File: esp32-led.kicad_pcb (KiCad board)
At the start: 2 copper layers, 28.7 x 55.6 mm, 10 parts, among them J1 LED Connector, J2 USB4125-GF-A_REVA2, J3 LED Connector, U1 SN74AHCT125D, U2 ESP32_NODEMCU

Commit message: Fixed issues, added gerber files
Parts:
- added REF**: MountingHole_4.3mm_M4_ISO14580, MountingHole:MountingHole_4.3mm_M4_ISO14580, F.Cu at (146.6, 95.2)
- added REF**: MountingHole_4.3mm_M4_ISO14580, MountingHole:MountingHole_4.3mm_M4_ISO14580, F.Cu at (146.7, 51.8)
- added REF**: MountingHole_4.3mm_M4_ISO14580, MountingHole:MountingHole_4.3mm_M4_ISO14580, F.Cu at (187.4, 95.1)
- added REF**: MountingHole_4.3mm_M4_ISO14580, MountingHole:MountingHole_4.3mm_M4_ISO14580, F.Cu at (187.4, 51.8)
- moved J1 0.32 mm to (164.6, 48.5)
- moved J3 0.20 mm to (169.7, 48.5)
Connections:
- J3 pad 1: +5V -> GND
- J3 pad 3: GND -> +5V
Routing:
- net DATA: track 28.6 -> 40.1 mm
- net +5V: track 100.5 -> 104.7 mm
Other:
- board size 28.7 x 55.6 mm -> 50.8 x 56.2 mm

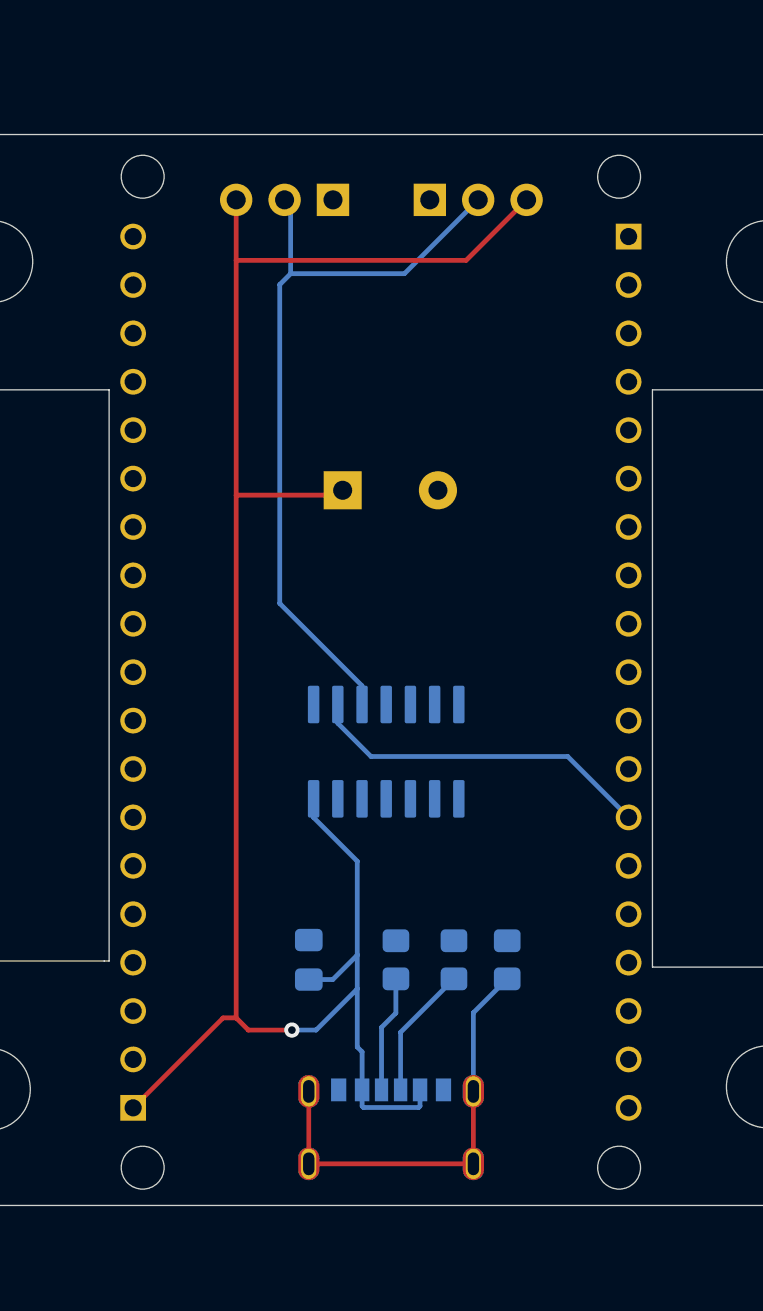
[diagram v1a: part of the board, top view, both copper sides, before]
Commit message: Chamged wrong esp32 footprint
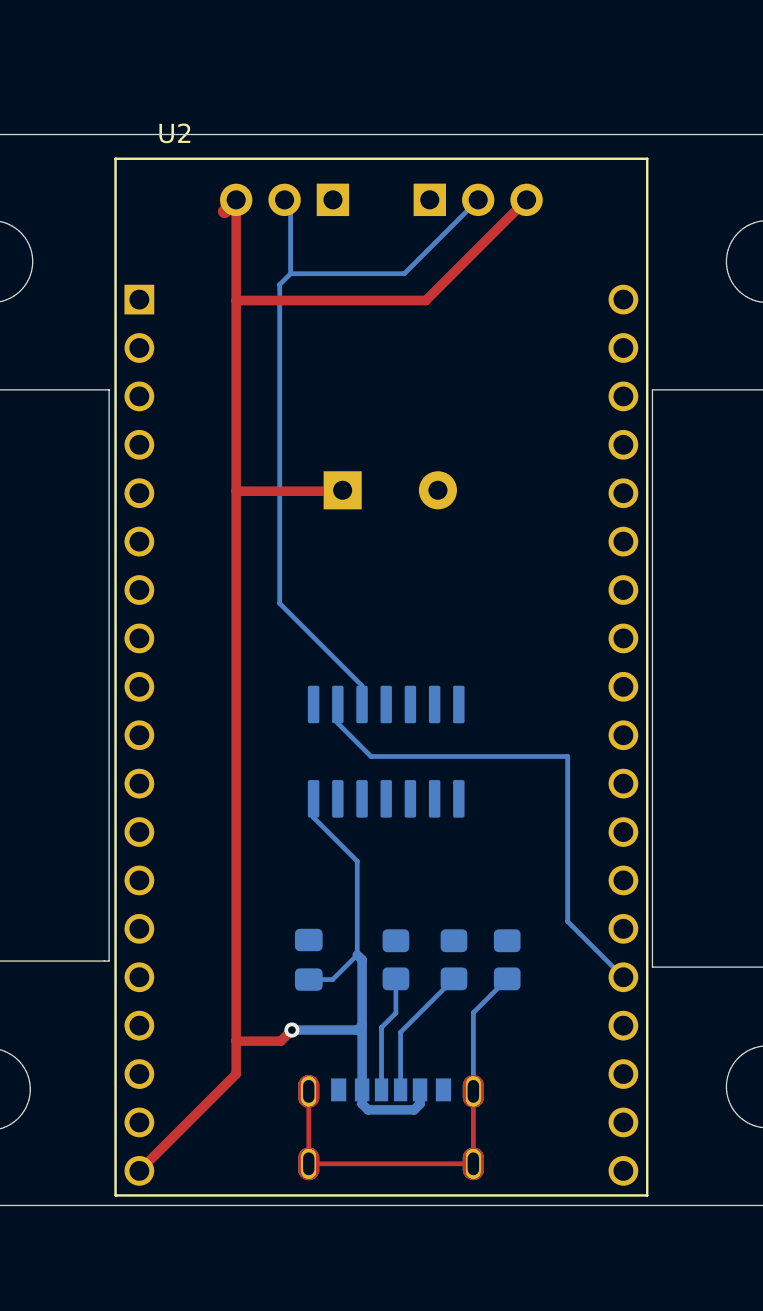
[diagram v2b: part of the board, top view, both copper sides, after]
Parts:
- U2: value ESP32_NODEMCU -> ESP32-DEVKITC-32D; footprint ESP32_NODEMCU:MODULE_ESP32_NODEMCU -> ESP32-DEVKITC-32D:MODULE_ESP32-DEVKITC-32D
- moved U2 0.21 mm to (167.1, 73.5)
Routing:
- net GPIO4: track 18.3 -> 26.6 mm
- net +5V: track 104.7 -> 109.1 mm
